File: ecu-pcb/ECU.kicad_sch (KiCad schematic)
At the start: 220 parts, among them J1 JTAG programming header, J3 USB-C receptacle, real Amphen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, J4 TE AMPSEAL 776180-1 (35-pos) 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, J5 TE AMPSEAL 776180-1 (35-pos) 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, J6 U.FL external BLE antenna con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, K1 Schrack RT1-16A-FormC (16A - 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, Q1 SQM40020EL_GE3 automotive (AE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, Q10 FGP3040G2 automotive ignition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, Q11 PMV37ENEA automotive (AEC-Q10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, Q12 PMV37ENEA automotive (AEC-Q10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, Q13 PMV37ENEA automotive (AEC-Q10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, Q14 PMV37ENEA automotive (AEC-Q10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, Q15 PMV37ENEA automotive (AEC-Q10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, Q16 PMV37ENEA automotive (AEC-Q10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, Q17 PMV37ENEA automotive (AEC-Q10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, Q18 PMV37ENEA automotive (AEC-Q10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, Q2 PMV230ENEA automotive (AEC-Q1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, Q3 FGP3040G2 automotive ignition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, Q4 FGP3040G2 automotive ignition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, Q5 FGP3040G2 automotive ignition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, Q6 FGP3040G2 automotive ignition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, Q7 FGP3040G2 automotive ignition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, Q8 FGP3040G2 automotive ignition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, Q9 FGP3040G2 automotive ignition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, U1 NXP MPC5606B automotive (Qori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, U10 TLV2372-Q1 automotive (AEC-Q1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, U11 NXP TJA1043T automotive CAN t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, U12 NXP TJA1043T automotive CAN t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, U13 FTDI FT4232HA automotive (AEC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, U14 TI CC2640R2F-Q1 automotive BL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, U15 TI SN3257-Q1 automotive 4ch a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, U16 MAX9924 automotive (AEC-Q100)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, U17 TLV2372-Q1 automotive (AEC-Q1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, U18 Bosch CJ125 wideband O2 contr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, U19 AD8495ARZ EGT amp (industrial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, U2 LM74700-Q1 (AEC-Q100 G1), U20 MC33926 ETC H-bridge (industr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, U3 LMR33630-Q1 (AEC-Q100 G1), U4 TLV733P-Q1 (AEC-Q100 G1), U5 ST L9779WD-SPI automotive (Mu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, U6 ST L9779WD-SPI automotive (Mu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, U7 MAX9924 automotive (AEC-Q100)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, U8 MAX9924 automotive (AEC-Q100)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, U9 Bosch CJ125 wideband O2 contr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, Y1 8MHz (AEC-Q200), Y2 12MHz (AEC-Q200), Y3 24MHz (AEC-Q200)

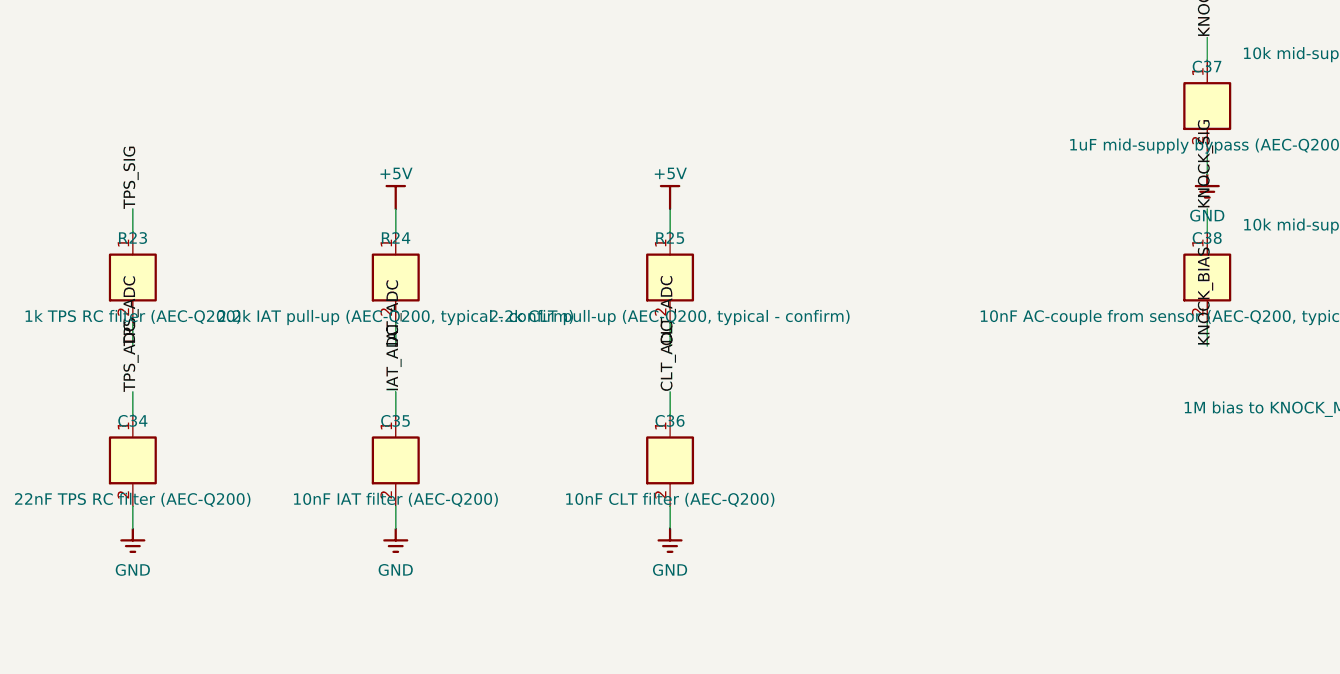
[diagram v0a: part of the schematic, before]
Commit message: Swap ECU CLT sensor to real GM-style resistive sending unit
Matches thermo-pcb's own engine-temperature sensor: DIYAutoTune's GM
Closed Element CLT/Oil Temperature Sensor, the same real part/curve
production automotive coolant senders use, rather than a generic
undocumented NTC placeholder. R25/C36 resized to thermo-pcb's own
proven values; new ecu-firmware clt_sensor.h/.c does the real
resistance->temperature lookup (piecewise-Beta table derived from the
sensor's 3 published calibration points, integer-only).

Also fixes a real latent bug found while touching this circuit: both
IAT's and CLT's pull-ups were wired to +5V despite this MCU's ADC
domain running at 3.3V (no separate VRH/VRL pins) - a real over-voltage
risk at cold temperatures. Both now pull up to +3V3. Board re-routed
and re-verified DRC-clean (only the same pre-existing, unrelated
findings remain).

Co-Authored-By: Claude Sonnet 5 <noreply@anthropic.com>
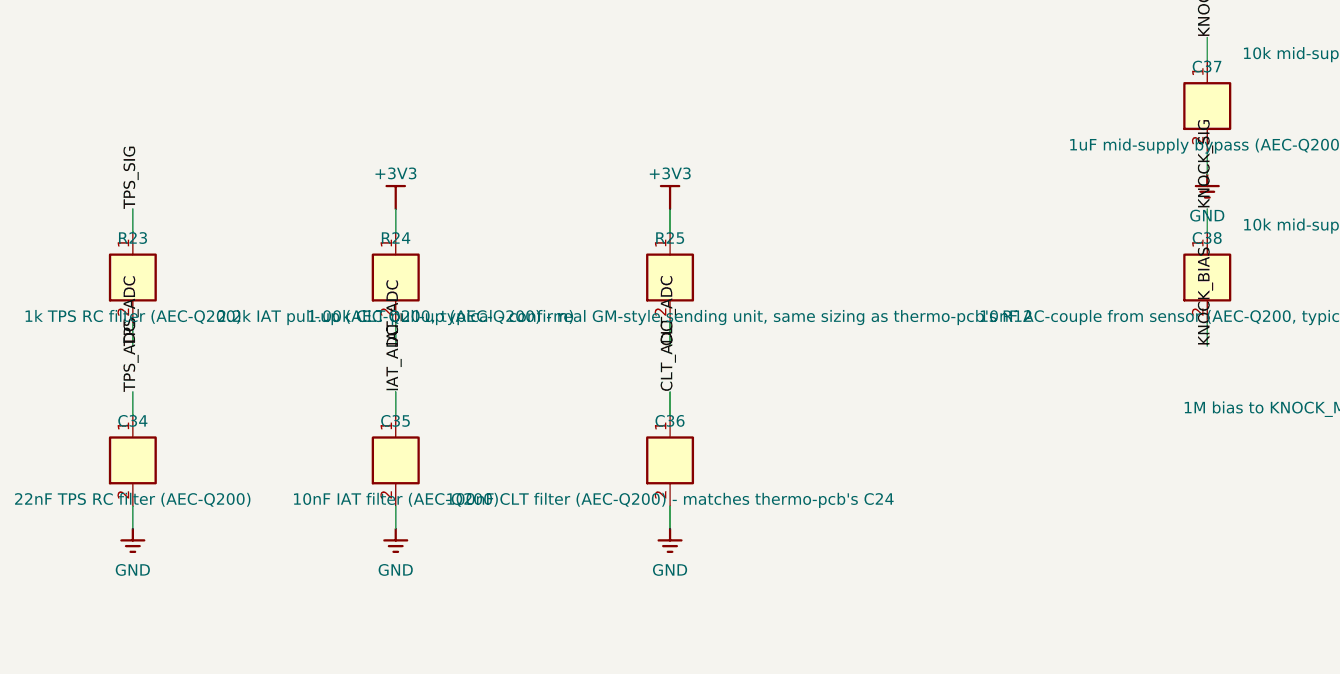
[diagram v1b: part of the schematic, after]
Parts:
- C36: value 10nF CLT filter (AEC-Q200) -> 100nF CLT filter (AEC-Q200) - matches thermo-pcb's C24
- R25: value 2.2k CLT pull-up (AEC-Q200, typical - confirm) -> 1.00k CLT pull-up (AEC-Q200) - real GM-style sending unit, same sizing as thermo-pcb's R12
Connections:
- net +3V3: now also R24.1, R25.1
- net +5V: no longer R24.1, R25.1

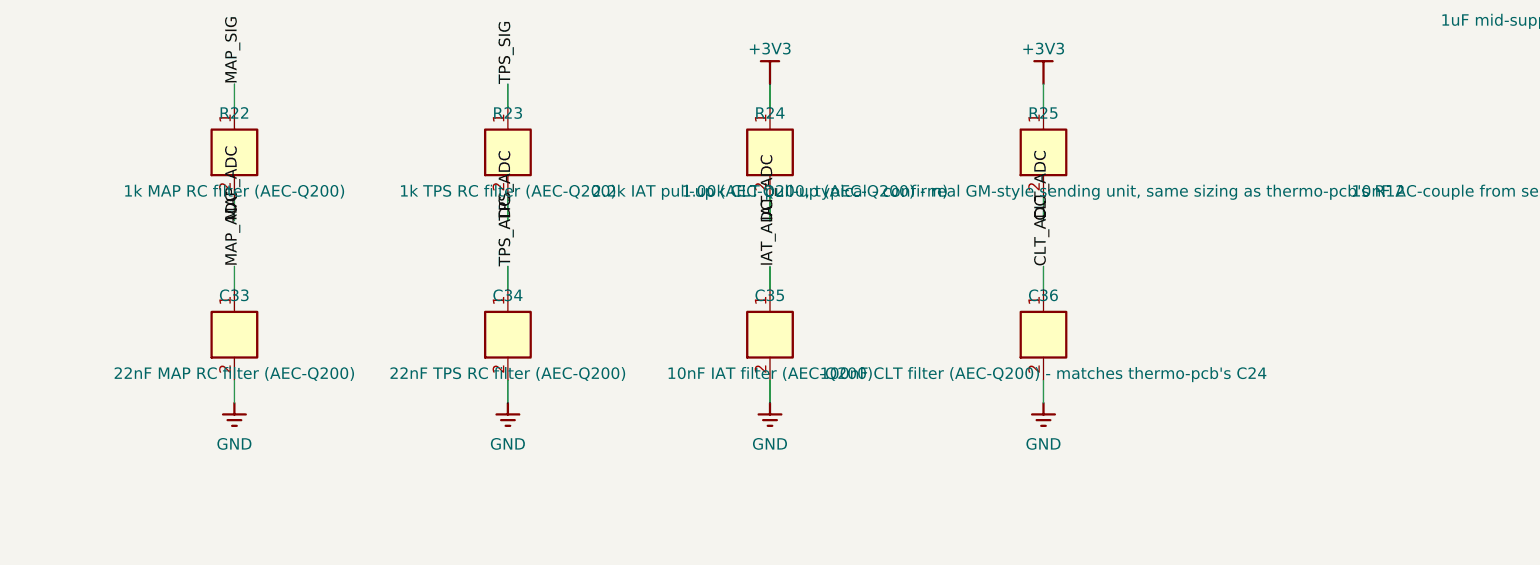
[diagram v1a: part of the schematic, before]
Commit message: Swap ECU IAT sensor to real GM-style open-element sensor
Same treatment as the CLT swap: DIYAutoTune's GM Open Element IAT
Temperature Sensor replaces the generic NTC placeholder. R24 resized to
4.22k (E96) via geometric-mean sizing across the sensor's full real
range, since intake air genuinely swings across nearly its whole span
in normal use (unlike thermostatically-regulated coolant). New
ecu-firmware iat_sensor.h/.c does the real conversion.

Found and resolved a real discrepancy while sourcing the part: the IAT
product page's own published curve agrees with CLT's curve at both
lower anchor points but disagrees on the third point's temperature for
the identical resistance reading. Traced to copy-paste content
contamination on the vendor's own site (a leftover "closed-element"
sentence on the IAT page, plus a physically implausible 2x jump in the
implied NTC Beta if the IAT page's own number were taken at face
value) - so iat_sensor.c reuses CLT's already cross-checked curve
rather than the likely-erroneous figure, documented inline.

Board re-routed and re-verified DRC-clean (only the same pre-existing,
unrelated findings remain).

Co-Authored-By: Claude Sonnet 5 <noreply@anthropic.com>
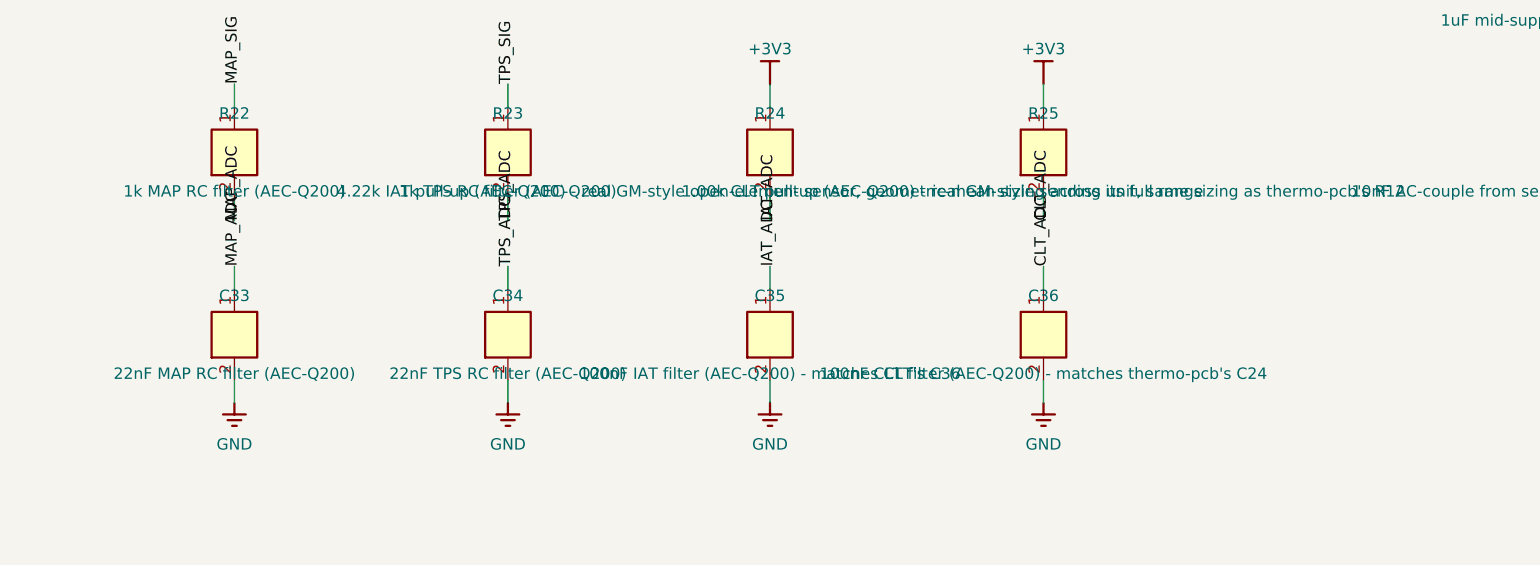
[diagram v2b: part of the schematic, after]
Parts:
- C35: value 10nF IAT filter (AEC-Q200) -> 100nF IAT filter (AEC-Q200) - matches CLT's C36
- R24: value 2.2k IAT pull-up (AEC-Q200, typical - confirm) -> 4.22k IAT pull-up (AEC-Q200) - real GM-style open-element sensor, geometric-mean sizing across its full range

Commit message: Fit L9779WD-SPI VDD5 regulator support - closes the ignition-drive gap
Reading the datasheet's Figure 3 and Table 13 showed the previously-
flagged CP/VDD_G gap was worse than the TODO wording admitted. Table 28
lists IGN1-4's own supply as VDD5, and VDD5 cannot exist without an
external NMOS pass transistor - the feature list says "5 V precision
voltage regulator with external NMOS" and Table 13 lists that NMOS and
a 100nF CP capacitor as required. So the board as drawn would have had
no ignition drive at all, not merely degraded drive.

Now fitted per chip: external pass NMOS (D to VB, G from VDD_G, S to
VDD5), 100nF CP-to-VB charge-pump cap (a bootstrap/flying cap, not to
ground), 10uF VDD5 cap and 1uF V3V3 cap - both inside Table 13's own
1-10uF ranges. D2PAK, not this board's usual SOT-23, because it is a
linear pass element burning ~1W per chip.

Verifying this also exposed a second real defect in the sourced rusEFI
footprint, visible only once the added parts shifted placement enough
for the router to pass a GND track underneath: an F.Mask polygon
duplicating the EPAD's own mask aperture plus two tabs extending past
the pad over bare copper - a real reflow solder-bridge hazard, caught
as a solder_mask_bridge DRC error. Removed. Same defect class as the
F.Cu polygon removed from this footprint during the migration.

Board re-routed: 0 unconnected items, only the 19 known-benign
lib_footprint_mismatch warnings. One open item recorded honestly - the
pass NMOS uses ST's own named testing reference (STD20NF06L) but its
AEC-Q101 status could not be confirmed, as every datasheet route
blocked or timed out this session.

Co-Authored-By: Claude Opus 5 <noreply@anthropic.com>
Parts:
- added C82, C83: 100nF CP charge-pump cap (AEC-Q200) - real Table 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, Capacitor_SMD:C_0603_1608Metric, symbol ECU:C_V
- added C84, C85: 10uF VDD5 reg cap (AEC-Q200) - real Table 13 rang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, Capacitor_SMD:C_0603_1608Metric, symbol ECU:C_V
- added C86, C87: 1uF V3V3 reg cap (AEC-Q200) - real Table 13 range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, Capacitor_SMD:C_0603_1608Metric, symbol ECU:C_V
- added Q20, Q21: STD20NF06L VDD5 ext pass NMOS (ST Table 13 testin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, Package_TO_SOT_SMD:TO-263-3_TabPin2, symbol ECU:MOSFET_N_BIG
- C19, C21: value 1uF VB decouple (AEC-Q200) - real value TBD, see comment -> 1uF VB/Cin reservoir (AEC-Q200) - place close to Q drain, see comment
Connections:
- net GND: now also C84.2, C85.2, C86.2, C87.2
- net VIN_PROT: now also C82.2, C83.2, Q20.3 (D), Q21.3 (D)
- net L9779_CP_0: now reaches U5.1 (CP)
- net L9779_CP_0: now also C82.1
- net L9779_VDDG_0: now reaches U5.2 (VDD_G)
- net L9779_VDDG_0: now also Q20.1 (G)
- net L9779_VDD5_0: now reaches U5.3 (VDD5)
- net L9779_VDD5_0: now also C84.1, Q20.2 (S)
- net L9779_V3V3_0: now reaches U5.4 (V3V3)
- net L9779_V3V3_0: now also C86.1
- net L9779_CP_1: now reaches U6.1 (CP)
- net L9779_CP_1: now also C83.1
- net L9779_VDDG_1: now reaches U6.2 (VDD_G)
- net L9779_VDDG_1: now also Q21.1 (G)
- net L9779_VDD5_1: now reaches U6.3 (VDD5)
- net L9779_VDD5_1: now also C85.1, Q21.2 (S)
- net L9779_V3V3_1: now reaches U6.4 (V3V3)
- net L9779_V3V3_1: now also C87.1
- no-connect marks 153 -> 145

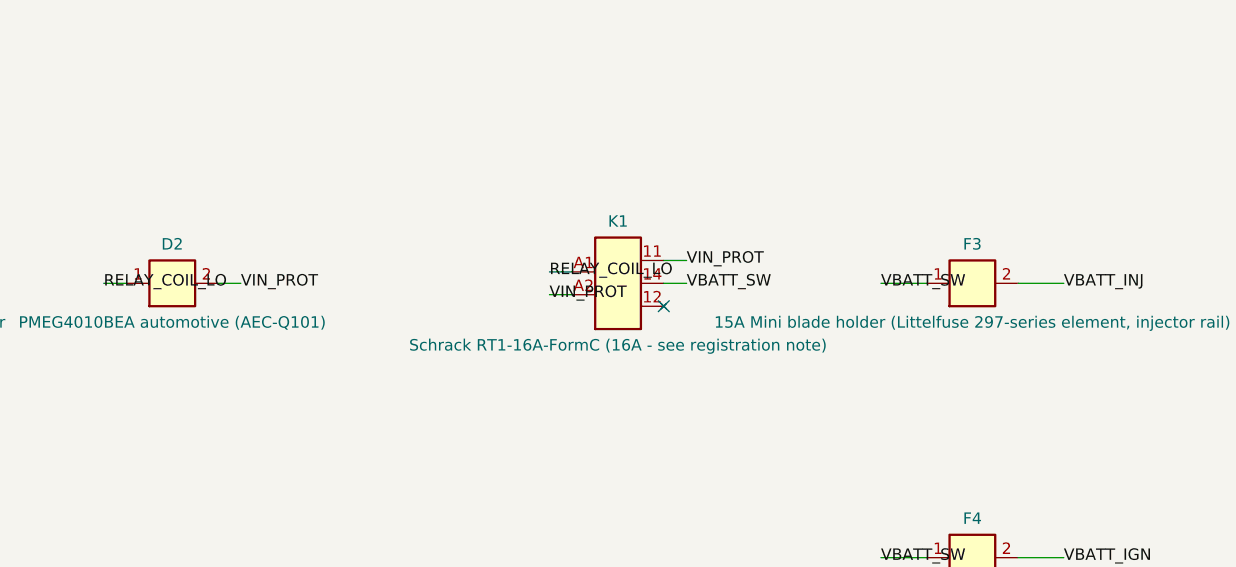
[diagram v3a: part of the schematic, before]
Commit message: Replace undersized K1 relay with 40A Panasonic CB1a-T-P-12V
K1 was a 16A Schrack RT1 sitting behind a 30A main fuse and carrying a
real ~22-28A switched load (injectors, ignition, O2 heater, ETC bridge,
VVT/idle/fuel-pump/boost - all downstream on VBATT_SW). Splitting into
two relays, the alternative the README suggested, was considered and
rejected on real numbers: the ignition branch alone (25A fuse, ~14-20A
draw) already exceeds a 16A relay, so splitting solves nothing.

Panasonic CB1a-T-P-12V instead: 1 Form A, 40A @ 14V DC, 40A continuous
carry at 85C, 2mOhm contacts, 12V/117mA coil, sealed. The -T suffix
matters - it gives -40..+125C, where the standard type is only +85C,
which is disqualifying for an engine bay. 40A now exceeds F1's 30A, so
the fuse is the weakest link rather than the relay.

No bundled KiCad footprint worked: every Relay_THT footprint was checked
for real pads and a >=30A rating, and the only one clearing both is an
EV/solar part rated to +85C. Also worth recording - both Potter&Brumfield
"12V30A" footprints self-describe as "Dummy for Space NO Pads", so the
trap that already bit this project once applies to the SPST variant too,
not only the SPDT. Footprint is therefore hand-built by a new
build_k1_footprint.py from Panasonic's own PC board pattern drawing,
with the derivation in its docstring - including the mirroring, which is
the one fatal detail: the pattern is bottom-view, KiCad is top-view, and
the pattern is asymmetric.

Two knock-on effects checked rather than assumed: the coil's real 117mA
is well within Q2's and D2's ratings, and the relay's 1A minimum
switching capacity is satisfied many times over.

Board re-routed and DRC-clean - violations down 19 to 18, since the
freshly generated footprint now matches its library exactly.

Co-Authored-By: Claude Opus 5 <noreply@anthropic.com>
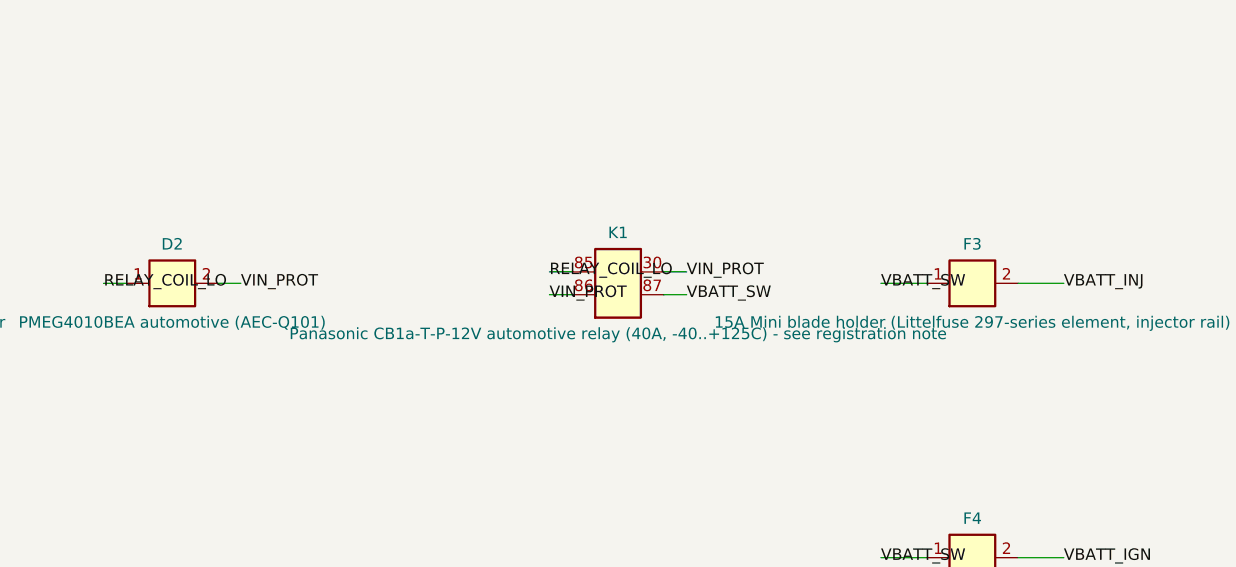
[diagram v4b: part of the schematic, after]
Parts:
- K1: value Schrack RT1-16A-FormC (16A - see registration note) -> Panasonic CB1a-T-P-12V automotive relay (40A, -40..+125C) - see registration note; footprint Relay_THT:Relay_SPDT_Schrack-RT1-16A-FormC_RM5mm -> panasonic:Panasonic_CB1a-T-P_Relay_40A
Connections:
- net RELAY_COIL_LO: now also K1.85 (COIL1); no longer K1.A1 (COIL1)
- net VBATT_SW: now also K1.87 (NO); no longer K1.14 (NO)
- net VIN_PROT: now also K1.30 (COM), K1.86 (COIL2); no longer K1.11 (COM), K1.A2 (COIL2)
- no-connect marks 145 -> 144
